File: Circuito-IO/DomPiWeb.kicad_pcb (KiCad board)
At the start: 2 copper layers, 110 x 65 mm, 120 parts, among them J1 CONUFL001-SMD-T (Linx), J10 Bx3, J11 Salida 5v, J12 Bateria 12v, J13 12v CA, J2 Salida 5v, J3 SIM7050-6-0-00-A, J4 RaspberryPi GPIO, J5 SIMDBG, J6 EXP1, J7 Bx2, J8 Bx3, J9 Bx2, Q1 DMG2305UXQ6, Q2 DMG2305UXQ6, U1 SIM900, U2 LM2596S-ADJ, U3 LM2596S-ADJ, U4 LM2596S-ADJ, U5 LM2596S-ADJ

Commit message: Update
Update
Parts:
- moved C1 2.00 mm to (156.4, 112.0)
- moved C2 2.00 mm to (156.5, 116.5)
- moved C20 2.00 mm to (141.0, 103.5)
- moved C21 2.00 mm to (123.5, 103.0)
- moved C3 2.00 mm to (156.8, 128.5)
- moved D12 2.00 mm to (165.0, 147.0)
- moved D16 2.00 mm to (165.0, 141.0)
- moved D3 2.00 mm to (156.8, 134.0)
- moved D4 2.00 mm to (156.2, 123.0)
- moved J12 2.00 mm to (169.5, 143.0)
- moved J5 2.00 mm to (175.0, 87.5)
- moved J6 2.00 mm to (150.5, 146.0)
- moved L2 2.00 mm to (133.0, 103.0)
- moved R15 2.00 mm to (175.0, 91.5)
- moved R30 2.00 mm to (172.5, 91.5)
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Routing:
- net GND: track 0.00 -> 23.3 mm, vias 0 -> 6
- net Net-(J4-Pad27): track 0.00 -> 17.4 mm
- net Net-(J4-Pad28): track 0.00 -> 12.8 mm
- net Net-(D13-Pad4): track 0.00 -> 10.5 mm
- net Net-(D13-Pad2): track 0.00 -> 10.5 mm
- net Net-(C6-Pad1): track 0.00 -> 10.0 mm
- net VBatSense: track 0.00 -> 7.70 mm
- net Net-(C4-Pad1): track 0.00 -> 6.01 mm
- net Net-(C7-Pad1): track 0.00 -> 5.63 mm
- net Net-(C15-Pad1): track 0.00 -> 5.01 mm
- net Net-(C12-Pad1): track 0.00 -> 5.01 mm
- net Net-(C10-Pad1): track 0.00 -> 5.01 mm
- net Net-(C17-Pad1): track 0.00 -> 4.99 mm
- net Net-(C11-Pad1): track 0.00 -> 4.96 mm
- net Net-(C16-Pad1): track 0.00 -> 4.94 mm
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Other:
- board size 110 x 65 mm -> 108 x 65 mm
- net class 1mm: clearance 0.3 -> 0.25
- net class Default: clearance 0.3 -> 0.25
- rule trace_clearance: 0.3 -> 0.25

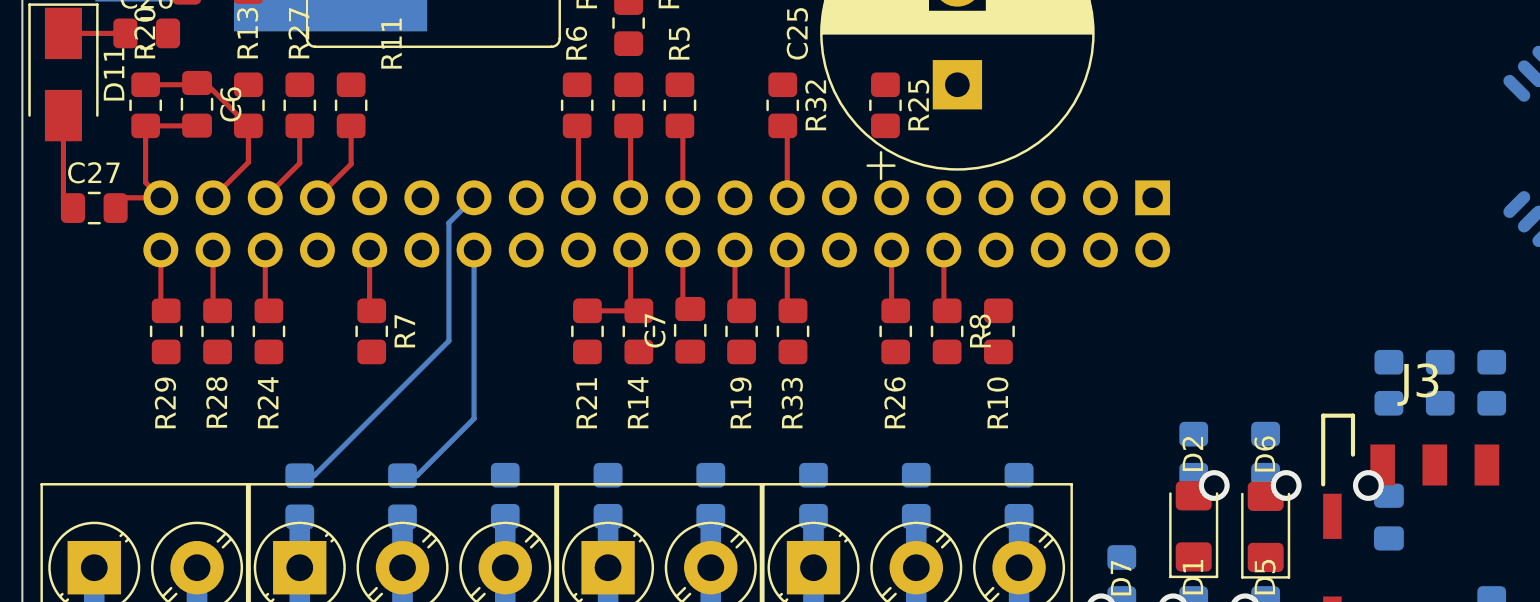
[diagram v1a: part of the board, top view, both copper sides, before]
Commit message: Desplazamiento 12mm de Raspberry Pi
Desplazamiento 12mm de Raspberry Pi
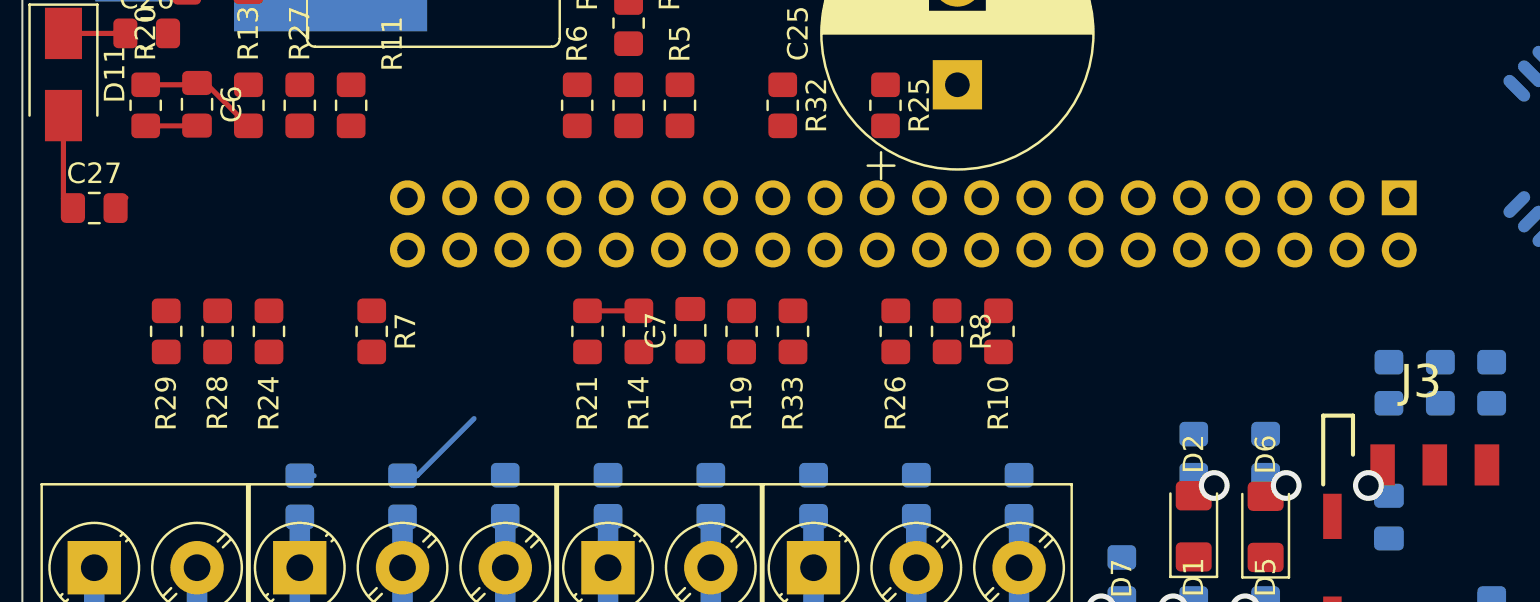
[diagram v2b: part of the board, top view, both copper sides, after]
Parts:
- moved J4 12.0 mm to (137.0, 125.0)
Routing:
- net Net-(J4-Pad27): track 17.4 -> 0.70 mm
- net Net-(J4-Pad28): track 12.8 -> 4.63 mm
- net GND: track 23.3 -> 15.3 mm
- net Net-(C6-Pad1): track 10.0 -> 5.83 mm
- net Net-(J4-Pad35): track 4.20 -> 0.00 mm
- net Net-(J4-Pad33): track 4.18 -> 0.00 mm
- net Net-(J4-Pad23): track 3.52 -> 0.08 mm
- net Net-(J4-Pad21): track 3.54 -> 0.14 mm
- net Net-(J4-Pad19): track 3.56 -> 0.20 mm
- net Net-(J4-Pad15): track 3.59 -> 0.31 mm
- net Net-(J4-Pad32): track 3.00 -> 0.14 mm
- net Net-(J4-Pad10): track 3.03 -> 0.23 mm
- net Net-(J4-Pad36): track 3.03 -> 0.25 mm
- net Net-(J4-Pad12): track 3.04 -> 0.28 mm
- net Net-(J4-Pad38): track 3.05 -> 0.31 mm
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
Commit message: Correccion
Correcciones por rotura y desincronización del repositorio
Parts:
- removed C18, C20, C22, C26, C27: 100nf, Capacitor_SMD:C_0805_2012Metric_Pad1.18x1.45mm_HandSolder
- removed C19, C21, C23, C28: 470uf, Capacitor_Tantalum_SMD:CP_EIA-7343-43_Kemet-X_Pad2.25x2.55mm_HandSolder
- removed C24: 33nf, Capacitor_SMD:C_0805_2012Metric_Pad1.18x1.45mm_HandSolder
- removed C25: 470uf / 25v, Capacitor_THT:CP_Radial_D13.0mm_P5.00mm
- removed the C6 at (78.5, 120.5)
- removed the C7 at (102.5, 131.4)
- removed the D10 at (159.7, 87.5)
- removed D11, D14: M7, Diode_SMD:D_SMA
- removed D12, D16: Led SMD, LED_SMD:LED_1206_3216Metric_Pad1.42x1.75mm_HandSolder
- removed D13: W10G, Diode_THT:Diode_Bridge_Round_D9.8mm
- removed D15: PMEG4050EP, Diode_SMD:D_SOD-128
- removed the D8 at (110.3, 87.5)
- removed the D9 at (133.8, 87.5)
- removed the J11 at (98.5, 92.0)
- removed the J12 at (169.5, 143.0)
- removed J13: 12v CA, TerminalBlock_Phoenix:TerminalBlock_Phoenix_PT-1,5-2-5.0-H_1x02_P5.00mm_Horizontal
- removed the J7 at (73.5, 143.0)
- removed L2, L3, L4: 47uH - SRR1210-470M, Inductor_SMD:L_Bourns_SRR1210A
- removed the R13 at (81.0, 120.5)
- removed the R14 at (100.0, 131.5)
- removed the R20 at (76.0, 120.5)
- removed the R21 at (97.5, 131.5)
- removed R43, R45, R47, R49, R51, R52: 1K, Resistor_SMD:R_0805_2012Metric_Pad1.20x1.40mm_HandSolder
- removed R44, R46: 3K3, Resistor_SMD:R_0805_2012Metric_Pad1.20x1.40mm_HandSolder
- removed R48: 2K2, Resistor_SMD:R_0805_2012Metric_Pad1.20x1.40mm_HandSolder
- removed R50: 10K, Resistor_SMD:R_0805_2012Metric_Pad1.20x1.40mm_HandSolder
- removed U3, U4, U5: LM2596S-ADJ, Package_TO_SOT_SMD:TO-263-5_TabPin3
- added C4: 100nf, Capacitor_SMD:C_0805_2012Metric_Pad1.18x1.45mm_HandSolder, F.Cu at (96.0, 101.0)
- added C5: 470uf, Capacitor_Tantalum_SMD:CP_EIA-7343-43_Kemet-X_Pad2.25x2.55mm_HandSolder, F.Cu at (96.0, 88.0)
- added D1: M7, Diode_SMD:D_SOD-128, F.Cu at (176.0, 113.5)
- added D3: M7, Diode_SMD:D_SOD-128, F.Cu at (171.6, 108.5)
- added D5: PMEG4050EP, Diode_SMD:D_SOD-128, F.Cu at (168.4, 113.8)
- added J1: Entrada 12v, TerminalBlock_Phoenix:TerminalBlock_Phoenix_PT-1,5-2-5.0-H_1x02_P5.00mm_Horizontal, F.Cu at (98.0, 72.0)
- added J2: Salida 5v, TerminalBlock_Phoenix:TerminalBlock_Phoenix_PT-1,5-2-5.0-H_1x02_P5.00mm_Horizontal, F.Cu at (118.0, 72.0)
- added J9: Bx2, TerminalBlock_Phoenix:TerminalBlock_Phoenix_PT-1,5-2-5.0-H_1x02_P5.00mm_Horizontal, F.Cu at (93.0, 113.0)
- added R2: 1K, Resistor_SMD:R_0805_2012Metric_Pad1.20x1.40mm_HandSolder, F.Cu at (98.5, 101.0)
- added R3: 3K3, Resistor_SMD:R_0805_2012Metric_Pad1.20x1.40mm_HandSolder, F.Cu at (93.5, 101.0)
- J4: renamed from J2; value Salida 5v -> Salida 5v Controlada
- R17: renamed from R12; moved to F.Cu
- U1: value SIM900 -> LM2596S-ADJ; footprint RF_GSM:SIMCom_SIM900 -> Package_TO_SOT_SMD:TO-263-5_TabPin3
- U2: value LM2596S-ADJ -> SIM900; footprint Package_TO_SOT_SMD:TO-263-5_TabPin3 -> RF_GSM:SIMCom_SIM900
- moved R4 81.5 mm to (165.0, 68.0), turned to 0 degrees
- moved J8 78.5 mm to (135.0, 69.0), turned to 270 degrees
- moved C8 75.3 mm to (137.5, 70.5), turned to 270 degrees
- moved U1 61.3 mm to (99.5, 101.0), turned to 180 degrees
- moved U2 51.1 mm to (160.0, 84.0), turned to 135 degrees
- moved J3 46.1 mm to (150.5, 68.5)
- moved R13 44.8 mm to (138.0, 93.0)
- moved R14 44.8 mm to (140.5, 93.0)
- moved R19 44.8 mm to (128.0, 93.0)
- moved R22 44.8 mm to (105.0, 93.0)
- moved R24 44.8 mm to (135.5, 93.0)
- moved R26 44.8 mm to (102.5, 93.0)
- moved R27 44.8 mm to (100.0, 93.0)
- moved R31 44.8 mm to (130.5, 93.0)
- moved R9 44.8 mm to (110.0, 93.0)
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- renumbered C4 to C6, C5 to C7, D7 to D10, D1 to D2, D2 to D4, D3 to D6, D4 to D7, D5 to D8, D6 to D9, J8 to J10, J9 to J11, J10 to J12, J1 to J3, J3 to J5, J4 to J6, J5 to J7, J6 to J8, R16 to R10, R17 to R11, R18 to R12, R8 to R13, R10 to R14, R9 to R15, R11 to R16, R15 to R18, R22 to R20, R23 to R21, R24 to R22, R25 to R23, R26 to R24, R27 to R25, R28 to R26, R29 to R27, R30 to R28, R31 to R29, R32 to R30, R33 to R31, R34 to R32, R35 to R33, R36 to R34, R37 to R35, R38 to R36, R39 to R37, R40 to R38, R41 to R39, R2 to R4, R42 to R40, R3 to R5, R4 to R6, R5 to R7, R6 to R8, R7 to R9
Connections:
- net +4V renamed Net-(D1-Pad1)
- C7 pad 1: Net-(C5-Pad1) -> Net-(C7-Pad1)
- D6 pad 2: Net-(D3-Pad2) -> Net-(D6-Pad2)
- D7 pad 2: Net-(D4-Pad2) (its old number) -> Net-(D7-Pad2)
- J3 pad 1: Net-(J1-Pad1) -> Net-(J3-Pad1)
- J5 pad C1: Net-(C5-Pad1) -> Net-(C7-Pad1)
- L1 pad 1: Net-(D8-Pad1) -> Net-(D5-Pad1)
- R10 pad 2: Net-(R16-Pad2) -> Net-(R10-Pad2)
- R11 pad 2: Net-(R17-Pad2) -> Net-(R11-Pad2)
- R12 pad 2: Net-(R18-Pad2) -> Net-(R12-Pad2)
- R13 pad 2: Net-(R8-Pad2) -> Net-(R13-Pad2)
- R14 pad 2: Net-(R10-Pad2) -> Net-(R14-Pad2)
- R15 pad 2: Net-(C5-Pad1) -> Net-(C7-Pad1)
- R20 pad 1: Net-(R22-Pad1) -> Net-(R20-Pad1)
- R21 pad 1: Net-(R23-Pad1) -> Net-(R21-Pad1)
- R28 pad 2: Net-(R30-Pad2) -> Net-(R28-Pad2)
- R29 pad 2: Net-(R31-Pad2) -> Net-(R29-Pad2)
- R6 pad 1: Net-(R4-Pad1) -> Net-(R6-Pad1)
- R7 pad 2: Net-(R4-Pad1) -> Net-(R6-Pad1)
- R9 pad 2: Net-(R7-Pad2) -> Net-(R9-Pad2)
- U1 pad 1: Net-(D4-Pad2) (its old number) -> Net-(D3-Pad1)
- U1 pad 2: Net-(U1-Pad2) -> Net-(D5-Pad1)
- U1 pad 4: Net-(R7-Pad2) -> Net-(R2-Pad1)
- U1 pad 5: Net-(U1-Pad5) -> GND
- U2 pad 1: Net-(C25-Pad1) -> Net-(D7-Pad2)
- U2 pad 2: Net-(D8-Pad1) -> Net-(U2-Pad2)
- U2 pad 4: Net-(R43-Pad1) -> Net-(R9-Pad2)
- U2 pad 5: GND -> Net-(U2-Pad5)
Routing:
- net GND: track 15.3 -> 0.00 mm, vias 6 -> 0
- net Net-(D13-Pad4): track 10.5 -> 0.00 mm
- net Net-(D13-Pad2): track 10.5 -> 0.00 mm
- net VBatSense: track 7.70 -> 0.00 mm
- net Net-(C6-Pad1): track 6.01 -> 0.00 mm
- net Net-(J6-Pad37): track 5.83 -> 0.00 mm
- net Net-(C15-Pad1): track 5.01 -> 0.00 mm
- net Net-(C12-Pad1): track 5.01 -> 0.00 mm
- net Net-(C10-Pad1): track 5.01 -> 0.00 mm
- net Net-(C17-Pad1): track 4.99 -> 0.00 mm
- net Net-(C11-Pad1): track 4.96 -> 0.00 mm
- net Net-(C16-Pad1): track 4.94 -> 0.00 mm
- net Net-(C14-Pad1): track 4.91 -> 0.00 mm
- net Net-(C13-Pad1): track 4.91 -> 0.00 mm
- net Net-(J6-Pad28): track 4.63 -> 0.00 mm
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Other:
- board size 108 x 65 mm -> 90 x 55 mm

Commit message: Lineas basicas
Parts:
- D3: moved to B.Cu
- J5: value SIM7050-6-0-00-A -> SIM7050
- Q2: moved to F.Cu
- moved D3 70.7 mm to (102.5, 93.5), turned to 180 degrees
- moved D5 59.9 mm to (110.0, 100.3), turned to 270 degrees
- moved D1 56.7 mm to (142.8, 67.5), turned to 180 degrees
- moved C5 38.6 mm to (132.5, 100.5), turned to 0 degrees
- moved C4 36.7 mm to (132.5, 104.5), turned to 0 degrees
- moved R3 17.6 mm to (110.5, 105.5), turned to 180 degrees
- moved D7 16.9 mm to (177.0, 81.7), turned to 90 degrees
- moved R4 13.5 mm to (151.5, 68.5)
- moved J3 13.5 mm to (164.0, 68.5)
- moved R17 13.1 mm to (112.5, 84.5), turned to 180 degrees
- moved Q1 10.1 mm to (151.5, 72.5), turned to 90 degrees
- moved J2 10.0 mm to (108.0, 72.0)
- moved J4 10.0 mm to (118.0, 72.0)
- moved R2 8.56 mm to (107.0, 102.0)
- moved C7 8.36 mm to (158.0, 114.0), turned to 0 degrees
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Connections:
- C8 pad 1: +5VA -> +5VD
- C9 pad 1: +5VA -> +5VD
- D1 pad 2: +5V -> +5VD
- J8 pad 1: +5VA -> +5VD
- J9 pad 1: +5VA -> +5VD
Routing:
- net +5VD: track 0.00 -> 164.2 mm
- net Net-(D3-Pad2): track 0.00 -> 25.0 mm
- net Net-(J8-Pad9): track 0.00 -> 23.7 mm
- net Net-(C1-Pad2): track 0.00 -> 22.3 mm, vias 0 -> 1
- net GND: track 0.00 -> 15.1 mm
- net Net-(D1-Pad1): track 0.00 -> 13.7 mm
- net Net-(J8-Pad4): track 0.00 -> 13.2 mm
- net Net-(C6-Pad1): track 0.00 -> 12.0 mm
- net Net-(D5-Pad1): track 0.00 -> 10.9 mm, vias 0 -> 1
- net Net-(D6-Pad2): track 0.00 -> 9.71 mm, vias 0 -> 1
- net Net-(C7-Pad1): track 0.00 -> 9.04 mm, vias 0 -> 2
- net Net-(R2-Pad1): track 0.00 -> 7.46 mm, vias 0 -> 1
- net Net-(C17-Pad1): track 0.00 -> 6.00 mm
- net Net-(C15-Pad1): track 0.00 -> 6.00 mm
- net Net-(C14-Pad1): track 0.00 -> 6.00 mm
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
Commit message: Correcciones al circuito
Correcciones al circuito
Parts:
- moved C10 2.50 mm to (135.5, 117.0)
- moved C11 2.50 mm to (130.5, 117.0)
- moved C12 2.50 mm to (125.5, 117.0)
- moved C13 2.50 mm to (120.5, 117.0)
- moved C14 2.50 mm to (115.5, 117.0)
- moved C15 2.50 mm to (110.5, 117.0)
- moved C16 2.50 mm to (105.5, 117.0)
- moved C17 2.50 mm to (100.5, 117.0)
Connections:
- J10 pad 1: Net-(C17-Pad1) -> Net-(J10-Pad1)
- J10 pad 2: Net-(C16-Pad1) -> Net-(J10-Pad2)
- J10 pad 3: Net-(C15-Pad1) -> Net-(J10-Pad3)
- J11 pad 1: Net-(C14-Pad1) -> Net-(J11-Pad1)
- J11 pad 2: Net-(C13-Pad1) -> Net-(J11-Pad2)
- J12 pad 1: Net-(C12-Pad1) -> Net-(J12-Pad1)
- J12 pad 2: Net-(C11-Pad1) -> Net-(J12-Pad2)
- J12 pad 3: Net-(C10-Pad1) -> Net-(J12-Pad3)
- J6 pad 26: Net-(J6-Pad26) -> Net-(C10-Pad1)
- J6 pad 27: Net-(J6-Pad27) -> Net-(C17-Pad1)
- J6 pad 28: Net-(J6-Pad28) -> Net-(C16-Pad1)
- J6 pad 29: Net-(J6-Pad29) -> Net-(C12-Pad1)
- J6 pad 3: Net-(J6-Pad3) -> Net-(C15-Pad1)
- J6 pad 31: Net-(J6-Pad31) -> Net-(C11-Pad1)
- J6 pad 5: Net-(J6-Pad5) -> Net-(C14-Pad1)
- J6 pad 7: Net-(J6-Pad7) -> Net-(C13-Pad1)
- R33 pad 1: Net-(C17-Pad1) -> Net-(J10-Pad1)
- R33 pad 2: Net-(J6-Pad27) -> Net-(C17-Pad1)
- R34 pad 1: Net-(C16-Pad1) -> Net-(J10-Pad2)
- R34 pad 2: Net-(J6-Pad28) -> Net-(C16-Pad1)
- R35 pad 1: Net-(C15-Pad1) -> Net-(J10-Pad3)
- R35 pad 2: Net-(J6-Pad3) -> Net-(C15-Pad1)
- R36 pad 1: Net-(C14-Pad1) -> Net-(J11-Pad1)
- R36 pad 2: Net-(J6-Pad5) -> Net-(C14-Pad1)
- R37 pad 1: Net-(C13-Pad1) -> Net-(J11-Pad2)
- R37 pad 2: Net-(J6-Pad7) -> Net-(C13-Pad1)
- R38 pad 1: Net-(C12-Pad1) -> Net-(J12-Pad1)
- R38 pad 2: Net-(J6-Pad29) -> Net-(C12-Pad1)
- R39 pad 1: Net-(C11-Pad1) -> Net-(J12-Pad2)
- R39 pad 2: Net-(J6-Pad31) -> Net-(C11-Pad1)
- R40 pad 1: Net-(C10-Pad1) -> Net-(J12-Pad3)
- R40 pad 2: Net-(J6-Pad26) -> Net-(C10-Pad1)
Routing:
- net Net-(D7-Pad1): track 0.00 -> 94.2 mm, vias 0 -> 2
- net Net-(R9-Pad2): track 0.00 -> 83.2 mm, vias 0 -> 3
- net Net-(R6-Pad1): track 0.00 -> 82.1 mm, vias 0 -> 3
- net Net-(C13-Pad1): track 6.00 -> 59.3 mm, vias 0 -> 2
- net Net-(C15-Pad1): track 6.00 -> 59.0 mm, vias 0 -> 2
- net Net-(D6-Pad1): track 0.00 -> 52.0 mm, vias 0 -> 2
- net Net-(J8-Pad7): track 0.00 -> 50.5 mm, vias 0 -> 1
- net Net-(R20-Pad1): track 0.00 -> 49.2 mm
- net Net-(C14-Pad1): track 6.00 -> 53.0 mm, vias 0 -> 2
- net Net-(J8-Pad3): track 0.00 -> 46.7 mm, vias 0 -> 1
- net Net-(J8-Pad8): track 0.00 -> 46.1 mm, vias 0 -> 1
- net Net-(R13-Pad2): track 0.00 -> 44.5 mm, vias 0 -> 1
- net Net-(R21-Pad1): track 0.00 -> 42.6 mm
- net Net-(C11-Pad1): track 5.96 -> 47.9 mm, vias 0 -> 2
- net Net-(R14-Pad2): track 0.00 -> 41.3 mm, vias 0 -> 1
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- added copper zone on B.Cu, net GND
- added copper zone on F.Cu, net GND

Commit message: Ajustes finales de Placa
Ajustes finales de Placa
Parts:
- moved C3 1.51 mm to (167.5, 88.8)
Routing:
- net Net-(R9-Pad2): track 83.2 -> 90.1 mm
- net Net-(R29-Pad2): track 34.8 -> 29.4 mm
- net Net-(R28-Pad2): track 35.3 -> 30.1 mm
- net Net-(J8-Pad9): track 23.7 -> 20.1 mm
- net Net-(C13-Pad1): track 59.3 -> 56.1 mm
- net Net-(R6-Pad1): track 82.1 -> 79.6 mm, vias 3 -> 4
- net Net-(C14-Pad1): track 53.0 -> 50.6 mm
- net Net-(R21-Pad1): track 42.6 -> 40.4 mm
- net Net-(J8-Pad10): track 28.8 -> 27.4 mm
- net Net-(D6-Pad1): track 52.0 -> 53.2 mm
- net Net-(J8-Pad3): track 46.7 -> 47.4 mm, vias 1 -> 2
- net Net-(D10-Pad2): track 2.42 -> 3.07 mm
- net Net-(C12-Pad1): track 44.5 -> 45.1 mm

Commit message: Maquillaje
Maquillaje
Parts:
- J1: value Entrada 12v -> 12V in
- J2: value Salida 5v -> 5V out
- J4: value Salida 5v Controlada -> 5v switch
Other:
- board text added: "ANTENA"
- board text added: "ARGENTINA"
- board text added: "DOMPIWEB"
- board text added: "EXPANCION"
- board text added: "HECHO EN"
- board text added: "SIM"
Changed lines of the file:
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@@
   (general
     (thickness 1.6)
-    (drawings 18)
+    (drawings 20)
     (tracks 584)
     (zones 0)
@@
       (effects (font (size 1 1) (thickness 0.15)))
     )
-    (fp_text value "Salida 5v" (at 2.5 6.06) (layer F.Fab)
+    (fp_text value "5V out" (at 2.5 5.91) (layer F.SilkS)
       (effects (font (size 1 1) (thickness 0.15)))
     )
@@
       (effects (font (size 1 1) (thickness 0.15)))
     )
-    (fp_text value "Entrada 12v" (at 2.5 6.06) (layer F.Fab)
+    (fp_text value "12V in" (at 2.5 5.91) (layer F.SilkS)
       (effects (font (size 1 1) (thickness 0.15)))
     )
@@
       (effects (font (size 1 1) (thickness 0.15)))
     )
-    (fp_text value "Salida 5v Controlada" (at 2.5 6.06 180) (layer F.Fab)
+    (fp_text value "5v switch" (at 2.5 5.91 180) (layer F.SilkS)
       (effects (font (size 1 1) (thickness 0.15)))
     )
@@
       (effects (font (size 1 1) (thickness 0.15)))
     )
-    (fp_text value SIMDBG (at 0 9.95 90) (layer F.Fab)
+    (fp_text value SIMDBG (at -2.25 3.8) (layer F.SilkS)
       (effects (font (size 1 1) (thickness 0.15)))
     )
@@
     )
   )
-  (dimension 32.6 (width 0.15) (layer F.SilkS)
-    (gr_text "32.600 mm" (at 86.800001 103.7 270) (layer F.SilkS)
-      (effects (font (size 1 1) (thickness 0.15)))
-    )
-    (feature1 (pts (xy 100 120) (xy 87.51358 120)))
-    (feature2 (pts (xy 100 87.4) (xy 87.51358 87.4)))
-    (crossbar (pts (xy 88.100001 87.4) (xy 88.100001 120)))
-    (arrow1a (pts (xy 88.100001 120) (xy 87.51358 118.873496)))
-    (arrow1b (pts (xy 88.100001 120) (xy 88.686422 118.873496)))
-    (arrow2a (pts (xy 88.100001 87.4) (xy 87.51358 88.526504)))
-    (arrow2b (pts (xy 88.100001 87.4) (xy 88.686422 88.526504)))
-  )
-  (dimension 10 (width 0.15) (layer F.SilkS)
-    (gr_text "10.000 mm" (at 95 61.8) (layer F.SilkS)
-      (effects (font (size 1 1) (thickness 0.15)))
-    )
-    (feature1 (pts (xy 90 87.4) (xy 90 62.513579)))
-    (feature2 (pts (xy 100 87.4) (xy 100 62.513579)))
-    (crossbar (pts (xy 100 63.1) (xy 90 63.1)))
-    (arrow1a (pts (xy 90 63.1) (xy 91.126504 62.513579)))
-    (arrow1b (pts (xy 90 63.1) (xy 91.126504 63.686421)))
-    (arrow2a (pts (xy 100 63.1) (xy 98.873496 62.513579)))
-    (arrow2b (pts (xy 100 63.1) (xy 98.873496 63.686421)))
-  )
-  (dimension 55 (width 0.15) (layer F.SilkS)
-    (gr_text "55.000 mm" (at 183.1 92.5 90) (layer F.SilkS)
-      (effects (font (size 1 1) (thickness 0.15)))
-    )
-    (feature1 (pts (xy 180 65) (xy 182.386421 65)))
-    (feature2 (pts (xy 180 120) (xy 182.386421 120)))
-    (crossbar (pts (xy 181.8 120) (xy 181.8 65)))
-    (arrow1a (pts (xy 181.8 65) (xy 182.386421 66.126504)))
-    (arrow1b (pts (xy 181.8 65) (xy 181.213579 66.126504)))
-    (arrow2a (pts (xy 181.8 120) (xy 182.386421 118.873496)))
-    (arrow2b (pts (xy 181.8 120) (xy 181.213579 118.873496)))
-  )
-  (dimension 90 (width 0.15) (layer F.SilkS)
-    (gr_text "90.000 mm" (at 135 125.1) (layer F.SilkS)
-      (effects (font (size 1 1) (thickness 0.15)))
-    )
-    (feature1 (pts (xy 90 120) (xy 90 124.386421)))
-    (feature2 (pts (xy 180 120) (xy 180 124.386421)))
-    (crossbar (pts (xy 180 123.8) (xy 90 123.8)))
-    (arrow1a (pts (xy 90 123.8) (xy 91.126504 123.213579)))
-    (arrow1b (pts (xy 90 123.8) (xy 91.126504 124.386421)))
-    (arrow2a (pts (xy 180 123.8) (xy 178.873496 123.213579)))
-    (arrow2b (pts (xy 180 123.8) (xy 178.873496 124.386421)))
+  (gr_text ANTENA (at 158.75 66.25) (layer F.SilkS)
+    (effects (font (size 1 1) (thickness 0.15)))
+  )
+  (gr_text SIM (at 169.35 110.75 90) (layer F.SilkS)
+    (effects (font (size 1 1) (thickness 0.15)))
+  )
+  (gr_text EXPANCION (at 136.25 80.95) (layer B.Cu)
+    (effects (font (size 1.5 1.5) (thickness 0.3)) (justify mirror))
+  )
+  (gr_text DOMPIWEB (at 136.25 78.9) (layer B.Cu)
+    (effects (font (size 1.5 1.5) (thickness 0.3)) (justify mirror))
+  )
+  (gr_text ARGENTINA (at 175.3 109.9 90) (layer F.Cu)
+    (effects (font (size 1.5 1.5) (thickness 0.3)))
+  )
+  (gr_text "HECHO EN" (at 172.3 110 90) (layer F.Cu)
+    (effects (font (size 1.5 1.5) (thickness 0.3)))
   )
   (gr_line (start 180 120) (end 90 120) (layer Edge.Cuts) (width 0.1))
@@
   (segment (start 133 113) (end 133 110) (width 1) (layer B.Cu) (net 120))
   (segment (start 128 113) (end 128 110) (width 1) (layer B.Cu) (net 121))
-  (zone (net 1) (net_name GND) (layer B.Cu) (hatch edge 0.508)
+  (zone (net 1) (net_name GND) (layer F.Cu) (hatch edge 0.508)
     (connect_pads (clearance 0.508))
     (min_thickness 0.254)
@@
     )
   )
-  (zone (net 1) (net_name GND) (layer F.Cu) (hatch edge 0.508)
+  (zone (net 1) (net_name GND) (layer B.Cu) (hatch edge 0.508)
     (connect_pads (clearance 0.508))
     (min_thickness 0.254)
